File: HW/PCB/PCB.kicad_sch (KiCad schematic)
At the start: 68 parts, among them J1 USB4105-GF-A, J4 Micro_SD_Card_Det_Hirose_DM3AT, Q2 SI1308EDL-T1-GE3, SW1 ssss213202, SW2 SKRPACE010, SW3 SKRPACE010, SW4 SKRPACE010, U1 BME280, U2 E-Paper 4.26inch, 800x480, U3 ESP32-S3-WROOM-1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

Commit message: change PCB design
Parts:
- C12: footprint TAJ_SMD:TAJB_AVX -> mylib:TAJB_AVX
- U2: footprint XF2M-2415-1A:CONN_XF2M-2415-1A_OMR -> mylib:CONN_XF2M-2415-1A_OMR
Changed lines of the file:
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@@
 (kicad_sch
-	(version 20231120)
+	(version 20250114)
 	(generator "eeschema")
-	(generator_version "8.0")
+	(generator_version "9.0")
 	(paper "A4")
 	(junction
@@
 			)
 		)
-		(property "Footprint" "TAJ_SMD:TAJB_AVX"
+		(property "Footprint" "mylib:TAJB_AVX"
 			(at 69.85 158.75 0)
 			(effects
@@
 			)
 		)
-		(property "Footprint" "XF2M-2415-1A:CONN_XF2M-2415-1A_OMR"
+		(property "Footprint" "mylib:CONN_XF2M-2415-1A_OMR"
 			(at 209.55 20.32 0)
 			(effects
@@
 		)
 	)
+	(embedded_fonts no)
 )

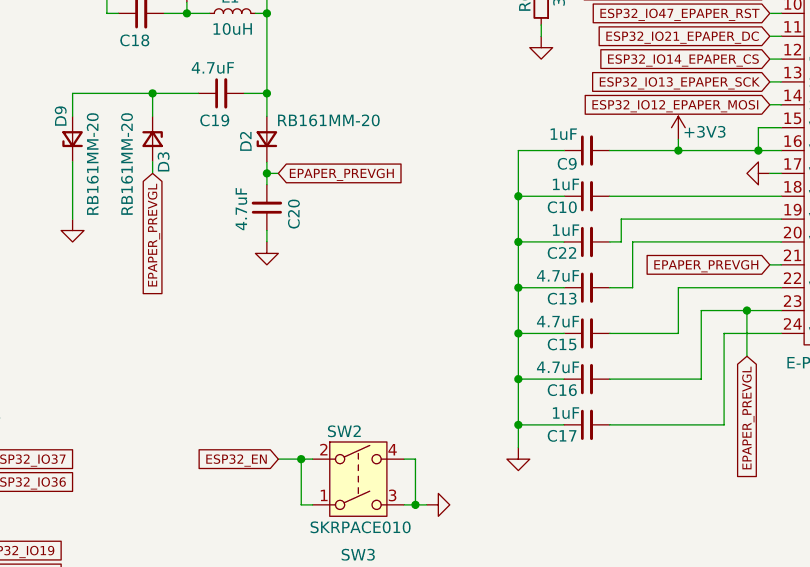
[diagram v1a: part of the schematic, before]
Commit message: change PCD layout
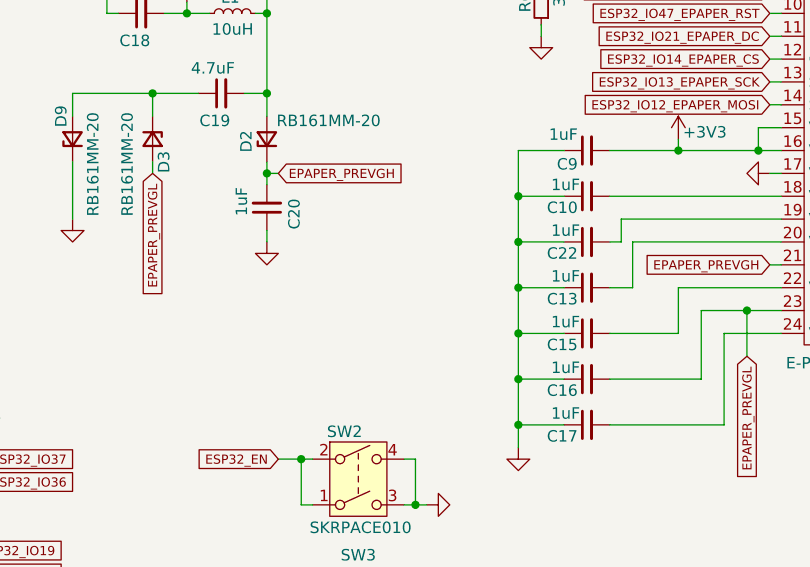
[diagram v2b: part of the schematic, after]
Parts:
- C10, C17, C22, C9: footprint Capacitor_SMD:C_0603_1608Metric_Pad1.08x0.95mm_HandSolder -> Capacitor_SMD:C_0805_2012Metric_Pad1.18x1.45mm_HandSolder
- C13, C15, C16, C20: value 4.7uF -> 1uF; footprint Capacitor_SMD:C_0603_1608Metric_Pad1.08x0.95mm_HandSolder -> Capacitor_SMD:C_0805_2012Metric_Pad1.18x1.45mm_HandSolder
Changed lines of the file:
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@@
 			)
 		)
-		(property "Footprint" "Capacitor_SMD:C_0603_1608Metric_Pad1.08x0.95mm_HandSolder"
+		(property "Footprint" "Capacitor_SMD:C_0805_2012Metric_Pad1.18x1.45mm_HandSolder"
 			(at 185.42 60.96 0)
 			(effects
@@
 			)
 		)
-		(property "Value" "4.7uF"
+		(property "Value" "1uF"
 			(at 184.658 80.01 90)
 			(effects
@@
 			)
 		)
-		(property "Footprint" "Capacitor_SMD:C_0603_1608Metric_Pad1.08x0.95mm_HandSolder"
+		(property "Footprint" "Capacitor_SMD:C_0805_2012Metric_Pad1.18x1.45mm_HandSolder"
 			(at 185.42 81.28 0)
 			(effects
@@
 			)
 		)
-		(property "Value" "4.7uF"
+		(property "Value" "1uF"
 			(at 147.066 59.944 90)
 			(effects
@@
 			)
 		)
-		(property "Footprint" "Capacitor_SMD:C_0603_1608Metric_Pad1.08x0.95mm_HandSolder"
+		(property "Footprint" "Capacitor_SMD:C_0805_2012Metric_Pad1.18x1.45mm_HandSolder"
 			(at 149.86 62.23 0)
 			(effects
@@
 			)
 		)
-		(property "Footprint" "Capacitor_SMD:C_0603_1608Metric_Pad1.08x0.95mm_HandSolder"
+		(property "Footprint" "Capacitor_SMD:C_0805_2012Metric_Pad1.18x1.45mm_HandSolder"
 			(at 185.42 66.04 0)
 			(effects
@@
 			)
 		)
-		(property "Value" "4.7uF"
+		(property "Value" "1uF"
 			(at 184.658 74.93 90)
 			(effects
@@
 			)
 		)
-		(property "Footprint" "Capacitor_SMD:C_0603_1608Metric_Pad1.08x0.95mm_HandSolder"
+		(property "Footprint" "Capacitor_SMD:C_0805_2012Metric_Pad1.18x1.45mm_HandSolder"
 			(at 185.42 76.2 0)
 			(effects
@@
 			)
 		)
-		(property "Footprint" "Capacitor_SMD:C_0603_1608Metric_Pad1.08x0.95mm_HandSolder"
+		(property "Footprint" "Capacitor_SMD:C_0805_2012Metric_Pad1.18x1.45mm_HandSolder"
 			(at 185.42 86.36 0)
 			(effects
@@
 			)
 		)
-		(property "Footprint" "Capacitor_SMD:C_0603_1608Metric_Pad1.08x0.95mm_HandSolder"
+		(property "Footprint" "Capacitor_SMD:C_0805_2012Metric_Pad1.18x1.45mm_HandSolder"
 			(at 185.42 55.88 0)
 			(effects
@@
 			)
 		)
-		(property "Value" "4.7uF"
+		(property "Value" "1uF"
 			(at 184.658 69.85 90)
 			(effects
@@
 			)
 		)
-		(property "Footprint" "Capacitor_SMD:C_0603_1608Metric_Pad1.08x0.95mm_HandSolder"
+		(property "Footprint" "Capacitor_SMD:C_0805_2012Metric_Pad1.18x1.45mm_HandSolder"
 			(at 185.42 71.12 0)
 			(effects
